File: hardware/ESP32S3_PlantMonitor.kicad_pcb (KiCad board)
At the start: 2 copper layers, 69 parts, among them J1 USB_C_Receptacle_USB2.0_16P, J2 Conn_01x03, J3 Conn_01x02, Q1 AO3401A, Q2 AO3401A, Q3 AO3401A, SW1 SW_Push, SW2 SW_Push, U1 USBLC6-2SC6, U2 AP2112K-3.3, U3 ESP32-S3-WROOM-1, U4 BME280, U5 VEML7700-TT, U6 MCP73831-2-OT

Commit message: Snapshot before 3D model path rework
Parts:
- D1: footprint Diode_SMD:D_SOD-123F -> PlantMonitor_JLC:D_SOD-123F
- D4: footprint Diode_SMD:D_SMA -> PlantMonitor_JLC:D_SMA
- F1: footprint Fuse:Fuse_1206_3216Metric -> PlantMonitor_JLC:Fuse_1206_3216Metric
- moved H1 132.9 mm to (34.6, 54.0)
- moved H3 132.1 mm to (35.9, 115.5)
- moved TP1 129.1 mm to (44.0, 52.6)
- moved TP2 129.1 mm to (44.0, 56.2)
- moved TP3 129.1 mm to (44.0, 59.8)
- moved TP4 129.1 mm to (44.0, 63.3)
- moved TP6 129.1 mm to (47.5, 56.2)
- moved TP7 129.1 mm to (47.5, 59.8)
- moved TP8 129.1 mm to (44.2, 67.1)
- moved TP5 123.4 mm to (53.3, 52.6)
- moved C13 113.9 mm to (66.2, 53.7)
- moved R8 113.9 mm to (66.2, 56.2)
- moved R9 113.9 mm to (66.2, 58.7)
- moved U5 109.1 mm to (73.5, 56.2)
- moved C5 106.3 mm to (76.8, 81.2)
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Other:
- board outline added: 78 x 70 mm
- board text added: "(BME280) 05_I2C_Sensors"
- board text added: "(veml7700) 05_I2C_Sensors"
- board text added: "02_USB_C_Input"
- board text added: "03_3V3_Power"
- board text added: "04_ESP32S3_Core"
- board text added: "06_Soil_Probe_Input"
- board text added: "07_Battery_PowerPath"

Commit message: Add 3D models for custom footprints
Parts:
- moved J1 3.60 mm to (32.8, 87.9)
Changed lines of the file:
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@@
 	)
 	(footprint "PlantMonitor_JLC:USB_C_Receptacle_HRO_TYPE-C-31-M-12"
-		(locked yes)
 		(layer "F.Cu")
-		(at 36.4 87.89 -90)
+		(at 32.8 87.89 -90)
 		(descr "USB Type-C receptacle for USB 2.0 and PD, http://www.krhro.com/uploads/soft/180320/1-1P320120243.pdf")
 		(tags "usb usb-c 2.0 pd")
@@
 		(model "${KIPRJMOD}/libs/PlantMonitor_JLC.3dshapes/HRO_TYPE-C-31-M-12.step"
 			(offset
-				(xyz -4.5 -3.5 0)
+				(xyz -4.5 -3.5 0.5)
 			)
 			(scale

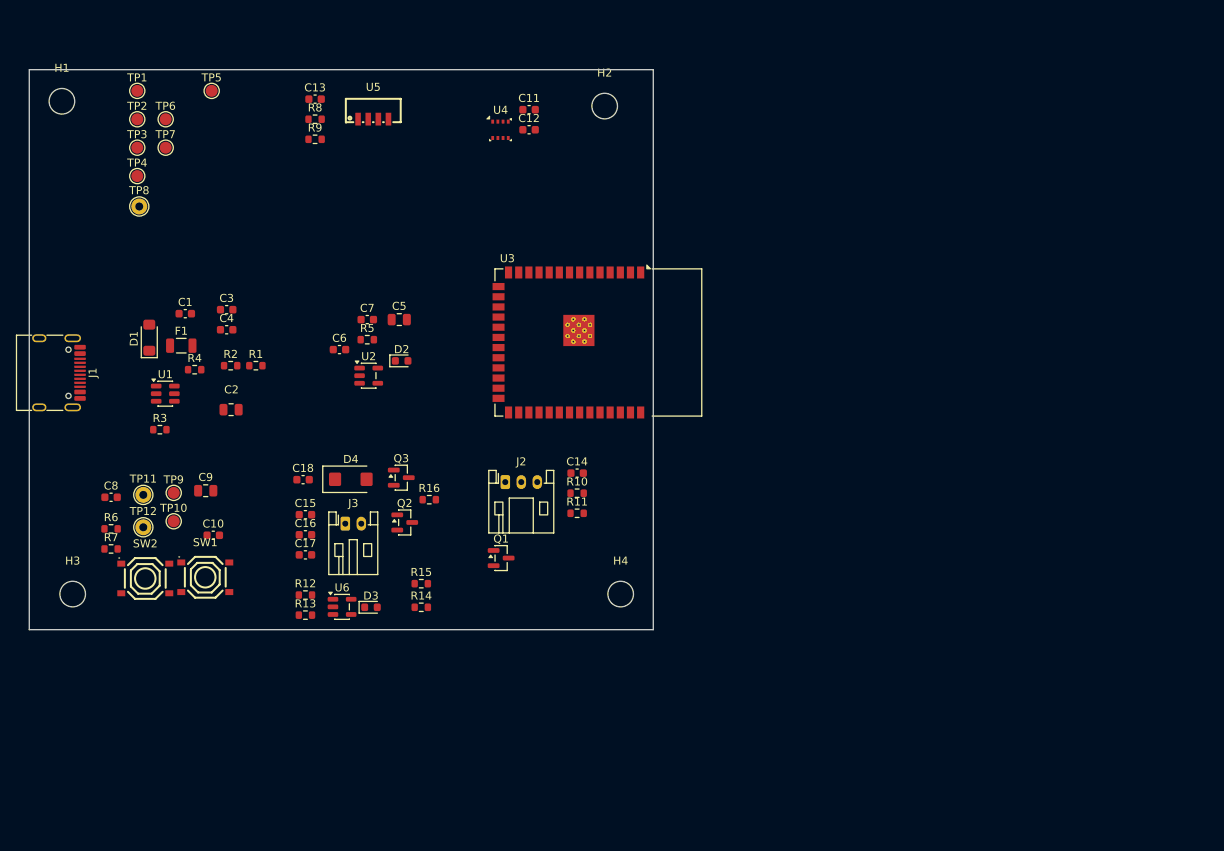
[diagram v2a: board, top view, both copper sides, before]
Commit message: Component placement: initial floorplan
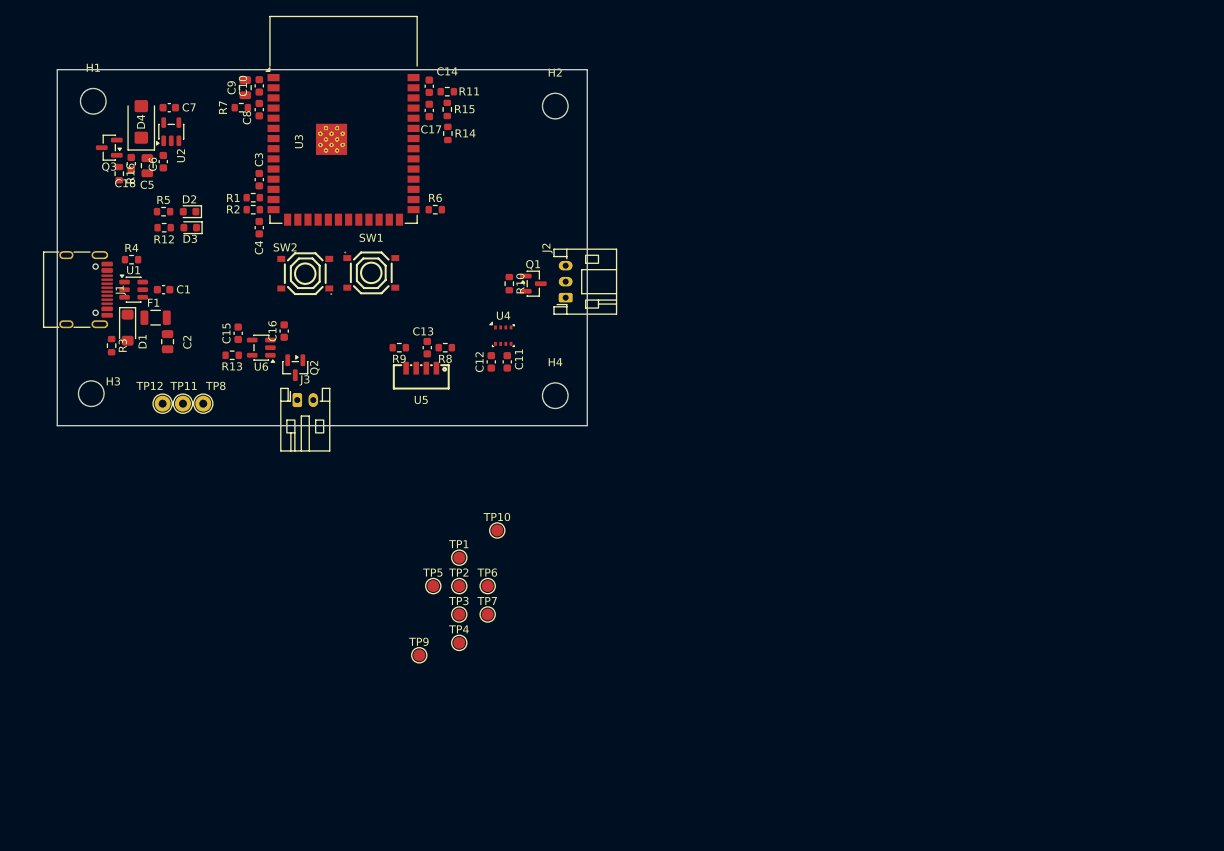
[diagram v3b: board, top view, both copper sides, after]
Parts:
- moved TP1 70.9 mm to (84.2, 111.0)
- moved TP4 70.9 mm to (84.2, 121.7)
- moved TP2 70.9 mm to (84.2, 114.5)
- moved TP3 70.9 mm to (84.2, 118.1)
- moved TP6 70.9 mm to (87.8, 114.5)
- moved TP7 70.9 mm to (87.8, 118.1)
- moved TP5 67.8 mm to (81.0, 114.5)
- moved R15 59.4 mm to (82.8, 55.0), turned to 90 degrees
- moved R14 59.3 mm to (82.8, 58.0), turned to 90 degrees
- moved C17 57.7 mm to (80.5, 55.1), turned to -90 degrees
- moved R7 57.5 mm to (57.0, 54.8), turned to 180 degrees
- moved R6 56.9 mm to (81.2, 67.5)
- moved C10 56.5 mm to (59.2, 52.0), turned to 90 degrees
- moved R16 56.2 mm to (41.8, 63.0), turned to -90 degrees
- moved R11 55.1 mm to (82.8, 52.8), turned to 180 degrees
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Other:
- board size 78 x 70 mm -> 66.2 x 44.5 mm
- board text removed: "(BME280) 05_I2C_Sensors"
- board text removed: "(veml7700) 05_I2C_Sensors"
- board text removed: "02_USB_C_Input"
- board text removed: "03_3V3_Power"
- board text removed: "04_ESP32S3_Core"
- board text removed: "06_Soil_Probe_Input"
- board text removed: "07_Battery_PowerPath"

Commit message: Placement refinements
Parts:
- turned SW1 to 180 degrees
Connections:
- SW1 pad 1: Net-(U3-IO0) -> GND
- SW1 pad 2: GND -> Net-(U3-IO0)
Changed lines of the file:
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@@
 	(footprint "PlantMonitor_JLC:SW-SMD_4P-L5.1-W5.1-P3.70-LS6.5-TL_H1.5"
 		(layer "F.Cu")
-		(at 73.25 75.4)
+		(at 73.25 75.4 180)
 		(property "Reference" "SW1"
-			(at 0 -4.35 0)
+			(at 0 3.65 0)
 			(layer "F.SilkS")
 			(effects
@@
 		(duplicate_pad_numbers_are_jumpers no)
 		(fp_line
-			(start -2.55 -1.17)
-			(end -2.55 1.17)
+			(start 2.55 -1.17)
+			(end 2.55 1.17)
 			(stroke
 				(width 0.25)
@@
 		)
 		(fp_line
-			(start -2.17 1.66)
-			(end -1.28 2.55)
+			(start 2.17 1.66)
+			(end 1.28 2.55)
 			(stroke
 				(width 0.25)
@@
 		)
 		(fp_line
-			(start -1.8 -1)
-			(end -1 -1.8)
+			(start 1.8 0.9)
+			(end 0.8 1.9)
 			(stroke
 				(width 0.25)
@@
 		)
 		(fp_line
-			(start -1.8 1)
-			(end -1.8 -1)
+			(start 1.8 -0.9)
+			(end 1.8 0.9)
 			(stroke
 				(width 0.25)
@@
 		)
 		(fp_line
-			(start -1.28 -2.55)
-			(end -2.17 -1.66)
+			(start 1.28 -2.55)
+			(end 2.17 -1.66)
 			(stroke
 				(width 0.25)
@@
 		)
 		(fp_line
-			(start -1.28 -2.55)
-			(end 1.28 -2.55)
+			(start 0.9 -1.8)
+			(end 1.8 -0.9)
 			(stroke
 				(width 0.25)
@@
 		)
 		(fp_line
-			(start -1.28 2.55)
-			(end 1.28 2.55)
+			(start 0.8 1.9)
+			(end -0.9 1.9)
 			(stroke
 				(width 0.25)
@@
 		)
 		(fp_line
-			(start -1 -1.8)
-			(end 0.9 -1.8)
+			(start -0.9 1.9)
+			(end -1.8 1)
 			(stroke
 				(width 0.25)
@@
 		)
 		(fp_line
-			(start -0.9 1.9)
-			(end -1.8 1)
+			(start -1 -1.8)
+			(end 0.9 -1.8)
 			(stroke
 				(width 0.25)
@@
 		)
 		(fp_line
-			(start 0.8 1.9)
-			(end -0.9 1.9)
+			(start -1.28 2.55)
+			(end 1.28 2.55)
 			(stroke
 				(width 0.25)
@@
 		)
 		(fp_line
-			(start 0.9 -1.8)
-			(end 1.8 -0.9)
+			(start -1.28 -2.55)
+			(end 1.28 -2.55)
 			(stroke
 				(width 0.25)
@@
 		)
 		(fp_line
-			(start 1.28 -2.55)
-			(end 2.17 -1.66)
+			(start -1.28 -2.55)
+			(end -2.17 -1.66)
 			(stroke
 				(width 0.25)
@@
 		)
 		(fp_line
-			(start 1.8 -0.9)
-			(end 1.8 0.9)
+			(start -1.8 1)
+			(end -1.8 -1)
 			(stroke
 				(width 0.25)
@@
 		)
 		(fp_line
-			(start 1.8 0.9)
-			(end 0.8 1.9)
+			(start -1.8 -1)
+			(end -1 -1.8)
 			(stroke
 				(width 0.25)
@@
 		)
 		(fp_line
-			(start 2.17 1.66)
-			(end 1.28 2.55)
+			(start -2.17 1.66)
+			(end -1.28 2.55)
 			(stroke
 				(width 0.25)
@@
 		)
 		(fp_line
-			(start 2.55 -1.17)
-			(end 2.55 1.17)
+			(start -2.55 -1.17)
+			(end -2.55 1.17)
 			(stroke
 				(width 0.25)
@@
 		)
 		(fp_circle
-			(center -3.25 -2.55)
-			(end -3.22 -2.55)
+			(center 0 0)
+			(end 1.28 0)
 			(stroke
-				(width 0.06)
+				(width 0.25)
 				(type solid)
 			)
@@
 		)
 		(fp_circle
-			(center 0 0)
-			(end 1.28 0)
+			(center -3.25 -2.55)
+			(end -3.22 -2.55)
 			(stroke
-				(width 0.25)
+				(width 0.06)
 				(type solid)
 			)
@@
 		)
 		(fp_line
-			(start -2.55 -1.3)
-			(end -1.3 -2.55)
+			(start 2.55 1.3)
+			(end 1.3 2.55)
 			(stroke
 				(width 0.05)
@@
 		)
 		(fp_line
-			(start -2.55 1.3)
-			(end -2.55 -1.3)
+			(start 2.55 -1.3)
+			(end 2.55 1.3)
 			(stroke
 				(width 0.05)
@@
 		)
 		(fp_line
-			(start -1.3 -2.55)
-			(end 1.3 -2.55)
+			(start 1.3 2.55)
+			(end -1.3 2.55)
 			(stroke
 				(width 0.05)
@@
 		)
 		(fp_line
-			(start -1.3 2.55)
-			(end -2.55 1.3)
+			(start 1.3 -2.55)
+			(end 2.55 -1.3)
 			(stroke
 				(width 0.05)
@@
 		)
 		(fp_line
-			(start 1.3 -2.55)
-			(end 2.55 -1.3)
+			(start -1.3 2.55)
+			(end -2.55 1.3)
 			(stroke
 				(width 0.05)
@@
 		)
 		(fp_line
-			(start 1.3 2.55)
-			(end -1.3 2.55)
+			(start -1.3 -2.55)
+			(end 1.3 -2.55)
 			(stroke
 				(width 0.05)
@@
 		)
 		(fp_line
-			(start 2.55 -1.3)
-			(end 2.55 1.3)
+			(start -2.55 1.3)
+			(end -2.55 -1.3)
 			(stroke
 				(width 0.05)
@@
 		)
 		(fp_line
-			(start 2.55 1.3)
-			(end 1.3 2.55)
+			(start -2.55 -1.3)
+			(end -1.3 -2.55)
 			(stroke
 				(width 0.05)
@@
 		)
 		(pad "1" smd rect
-			(at -3 -1.85)
+			(at -3 -1.85 180)
 			(size 1 0.75)
 			(layers "F.Cu" "F.Mask" "F.Paste")
-			(net "Net-(U3-IO0)")
+			(net "GND")
 			(pinfunction "1_1")
 			(pintype "passive")
 		)
 		(pad "1" smd rect
-			(at 3 -1.85)
+			(at 3 -1.85 180)
 			(size 1 0.75)
 			(layers "F.Cu" "F.Mask" "F.Paste")
-			(net "Net-(U3-IO0)")
+			(net "GND")
 			(pinfunction "1_1")
 			(pintype "passive")
 		)
 		(pad "2" smd rect
-			(at -3 1.85)
+			(at -3 1.85 180)
 			(size 1 0.75)
 			(layers "F.Cu" "F.Mask" "F.Paste")
-			(net "GND")
+			(net "Net-(U3-IO0)")
 			(pinfunction "2_2")
 			(pintype "passive")
 		)
 		(pad "2" smd rect
-			(at 3 1.85)
+			(at 3 1.85 180)
 			(size 1 0.75)
 			(layers "F.Cu" "F.Mask" "F.Paste")
-			(net "GND")
+			(net "Net-(U3-IO0)")
 			(pinfunction "2_2")
 			(pintype "passive")
@@
 		(at 65 75.5 180)
 		(property "Reference" "SW2"
-			(at 2.5 3.25 0)
+			(at 0 3.75 0)
 			(layer "F.SilkS")
 			(effects

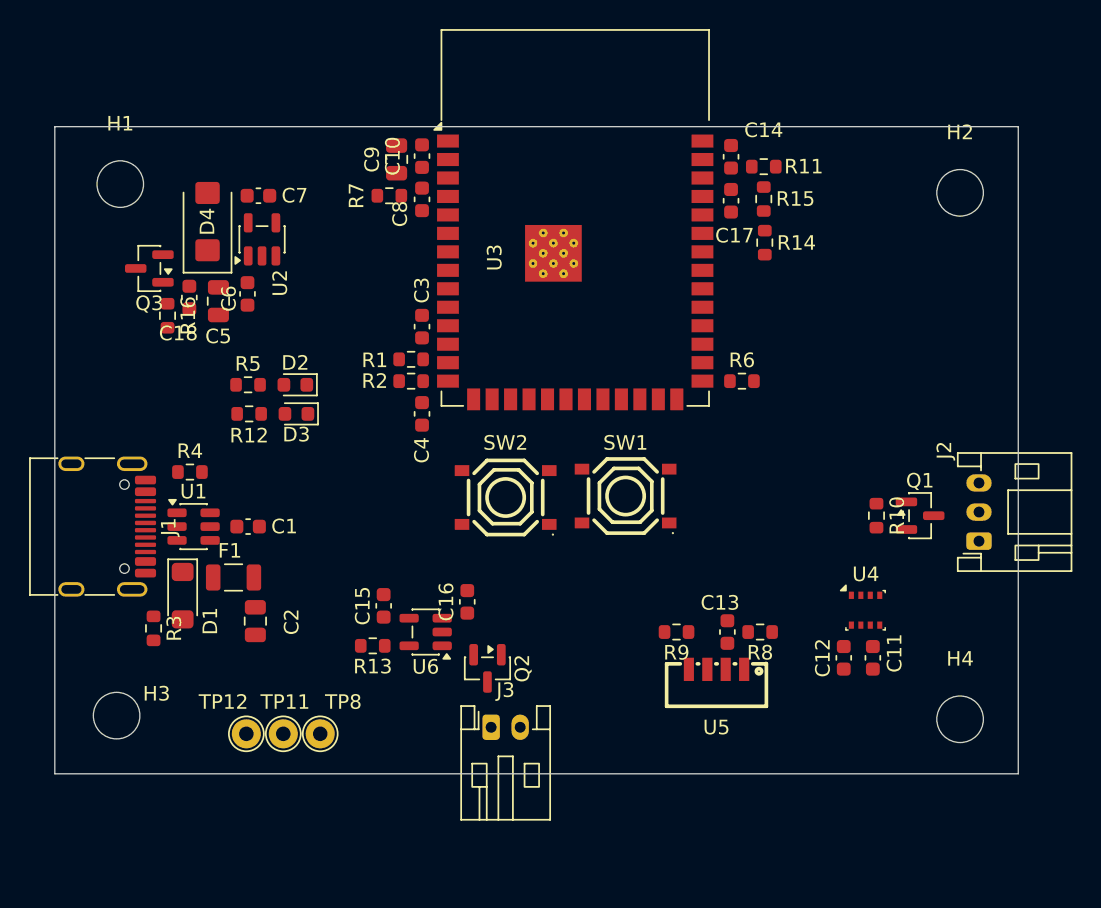
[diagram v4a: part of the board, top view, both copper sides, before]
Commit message: Placement fixes; rounded board corners (R4.25)
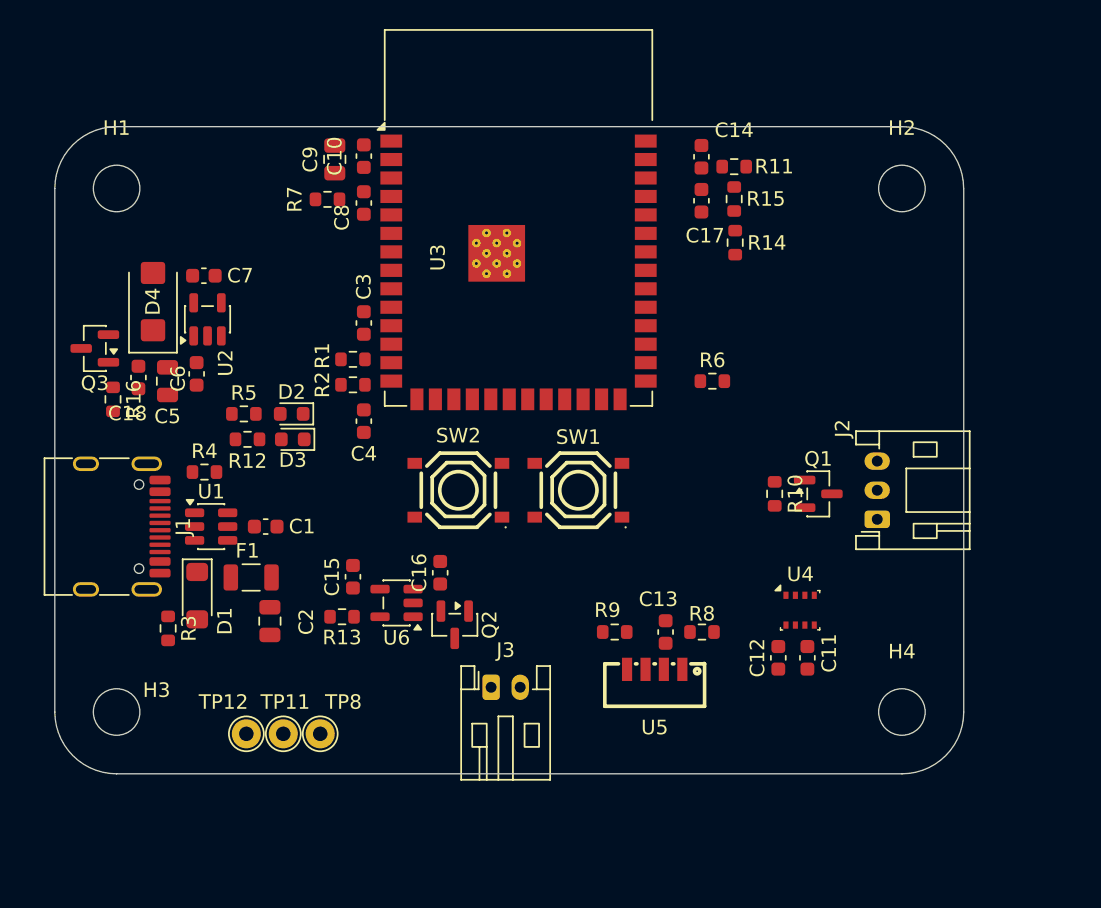
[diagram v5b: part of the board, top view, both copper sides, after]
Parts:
- moved J2 7.16 mm to (90.5, 77.0)
- moved Q1 7.16 mm to (86.5, 75.2)
- moved R10 7.16 mm to (83.5, 75.2)
- moved R16 6.86 mm to (38.0, 68.8)
- moved C7 6.66 mm to (44.2, 60.2)
- moved D4 6.66 mm to (40.8, 62.0)
- moved Q3 6.66 mm to (36.8, 65.2)
- moved U2 6.66 mm to (44.5, 63.2)
- moved C18 6.52 mm to (39.8, 67.2)
- moved C5 6.52 mm to (41.8, 67.5)
- moved C6 6.52 mm to (43.8, 67.0)
- moved C11 4.50 mm to (85.8, 86.5)
- moved C12 4.50 mm to (83.8, 86.5)
- moved U4 4.50 mm to (85.2, 83.2)
- moved R7 4.26 mm to (52.8, 55.0)
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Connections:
- net Net-(J1-D+-PadA6) renamed /02_USB_C_Input/USB_CONN_DP
- net Net-(J1-D--PadA7) renamed /02_USB_C_Input/USB_CONN_DN
- net Net-(R1-Pad1) renamed /02_USB_C_Input/USB_ESD_DN
- net Net-(R2-Pad1) renamed /02_USB_C_Input/USB_ESD_DP
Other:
- board size 66.2 x 44.5 mm -> 62.5 x 44.5 mm

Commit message: Routing: bulk of nets complete
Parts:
- moved SW2 32.3 mm to (92.0, 63.6), turned to 0 degrees
- moved TP4 23.9 mm to (106.5, 112.8)
- moved TP1 23.9 mm to (106.5, 102.2)
- moved TP2 23.9 mm to (106.5, 105.8)
- moved TP3 23.9 mm to (106.5, 109.3)
- moved TP5 23.9 mm to (103.2, 105.8)
- moved TP6 23.9 mm to (110.0, 105.8)
- moved TP7 23.9 mm to (110.0, 109.3)
- moved TP9 23.9 mm to (101.5, 114.4)
- moved TP10 20.7 mm to (105.2, 94.8)
- moved J2 20.4 mm to (73.8, 88.5), turned to 0 degrees
- moved SW1 17.9 mm to (83.8, 63.6), turned to 0 degrees
- moved U5 17.7 mm to (92.0, 81.5), turned to -90 degrees
- moved R9 17.7 mm to (90.2, 84.5), turned to -90 degrees
- moved R5 16.7 mm to (62.3, 76.5), turned to 180 degrees
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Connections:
- net Net-(U3-EN) renamed /04_ESP32S3_Core/EN
- net Net-(U3-IO0) renamed /04_ESP32S3_Core/BOOT
- net Net-(U3-RXD0) renamed /04_ESP32S3_Core/RXD0
- net Net-(U3-TXD0) renamed /04_ESP32S3_Core/TXD0
- U3 pad 31: unconnected-(U3-IO38-Pad31) -> SDA
- U3 pad 32: unconnected-(U3-IO39-Pad32) -> SCL
- U3 pad 4: SCL -> unconnected-(U3-IO4-Pad4)
- U3 pad 5: SDA -> unconnected-(U3-IO5-Pad5)
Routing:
- net +3V3: track 0.00 -> 113.0 mm, vias 0 -> 5
- net +5V_PROT: track 0.00 -> 72.4 mm, vias 0 -> 3
- net VBAT: track 0.00 -> 71.6 mm, vias 0 -> 3
- net /04_ESP32S3_Core/TXD0: track 0.00 -> 54.7 mm, vias 0 -> 2
- net GND: track 0.00 -> 51.7 mm, vias 0 -> 22
- net /04_ESP32S3_Core/RXD0: track 0.00 -> 51.6 mm, vias 0 -> 2
- net /04_ESP32S3_Core/EN: track 0.00 -> 47.7 mm, vias 0 -> 2
- net ADC_SOIL: track 0.00 -> 43.5 mm, vias 0 -> 2
- net SDA: track 0.00 -> 35.1 mm, vias 0 -> 3
- net /02_USB_C_Input/USB_VBUS: track 0.00 -> 32.1 mm, vias 0 -> 5
- net SCL: track 0.00 -> 31.5 mm, vias 0 -> 4
- net Net-(D3-K): track 0.00 -> 26.5 mm
- net VSYS: track 0.00 -> 19.5 mm
- net SENS_PWR_EN: track 0.00 -> 14.7 mm, vias 0 -> 2
- net /04_ESP32S3_Core/BOOT: track 0.00 -> 14.2 mm, vias 0 -> 2
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- added copper zone on In1.Cu, net GND
- added copper zone on In2.Cu, net GND
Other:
- copper layers 2 -> 4
- board text added: "+"
- board text added: "-"
- board text added: "3V3"
- board text added: "5V"
- board text added: "BAT"
- board text added: "BAT_SNS"
- board text added: "BME280"
- board text added: "BOOT"
- board text added: "CHG"
- board text added: "EN"
- board text added: "ESP32-S3"
- board text added: "GND"
- board text added: "IO0"
- board text added: "LDO"
- board text added: "LED indicators"
- board text added: "LIGHT SENSOR"
- board text added: "PWR"
- board text added: "RESET"
- board text added: "RX"
- board text added: "SIG"
- board text added: "SOIL"
- board text added: "SOIL_ADC"
- board text added: "TX"
- board text added: "UART"
- board text added: "USB"
- board text added: "USB-C"
- board text added: "VBAT"
- board text added: "VEML7700"
- board text added: "VSYS"
- board text added: "battery charger"
- board text added: "soil sensor"

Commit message: Routing complete pending cleanup
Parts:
- moved TP3 81.9 mm to (46.9, 53.0)
- moved TP9 72.3 mm to (52.5, 61.2)
- moved TP2 69.6 mm to (50.0, 65.1)
- moved TP1 58.2 mm to (50.5, 86.1)
- moved TP7 57.1 mm to (87.0, 57.1)
- moved TP5 56.0 mm to (81.8, 54.0)
- moved TP4 52.3 mm to (69.2, 76.2)
- moved TP6 28.7 mm to (85.0, 91.7)
- moved TP10 28.4 mm to (83.6, 76.3)
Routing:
- net ADC_SOIL: track 43.5 -> 57.1 mm
- net /04_ESP32S3_Core/BOOT: track 14.2 -> 26.8 mm, vias 2 -> 4
- net +3V3: track 113.0 -> 121.8 mm, vias 5 -> 7
- net BAT_SENSE: track 7.09 -> 14.9 mm, vias 0 -> 2
- net /04_ESP32S3_Core/EN: track 47.7 -> 55.0 mm
- net +5V_PROT: track 72.4 -> 78.8 mm, vias 3 -> 4
- net VBAT: track 71.6 -> 77.4 mm, vias 3 -> 4
- net GND: track 51.7 -> 56.4 mm
- net /02_USB_C_Input/USB_VBUS: track 32.1 -> 27.8 mm
- net VSYS: track 19.5 -> 23.2 mm
